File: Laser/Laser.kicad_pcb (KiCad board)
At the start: 2 copper layers, 25.4 x 25.4 mm, 2 parts, among them J1 Laser Diode, J2 Conn_01x03

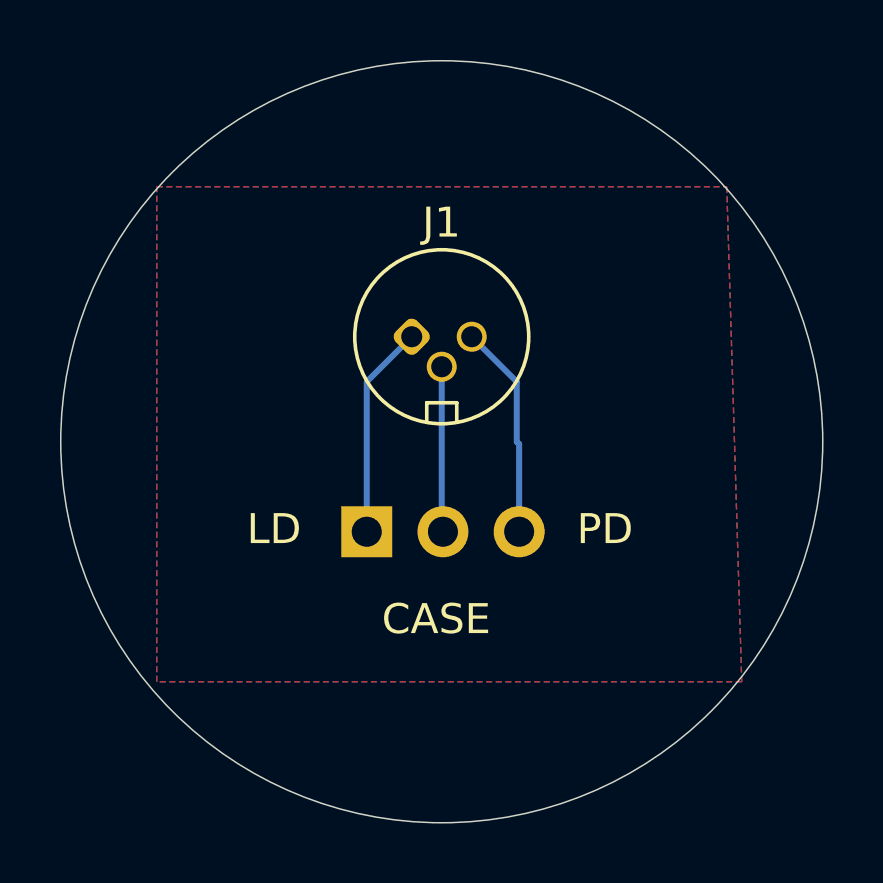
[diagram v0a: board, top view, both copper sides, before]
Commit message: Centering laser diode
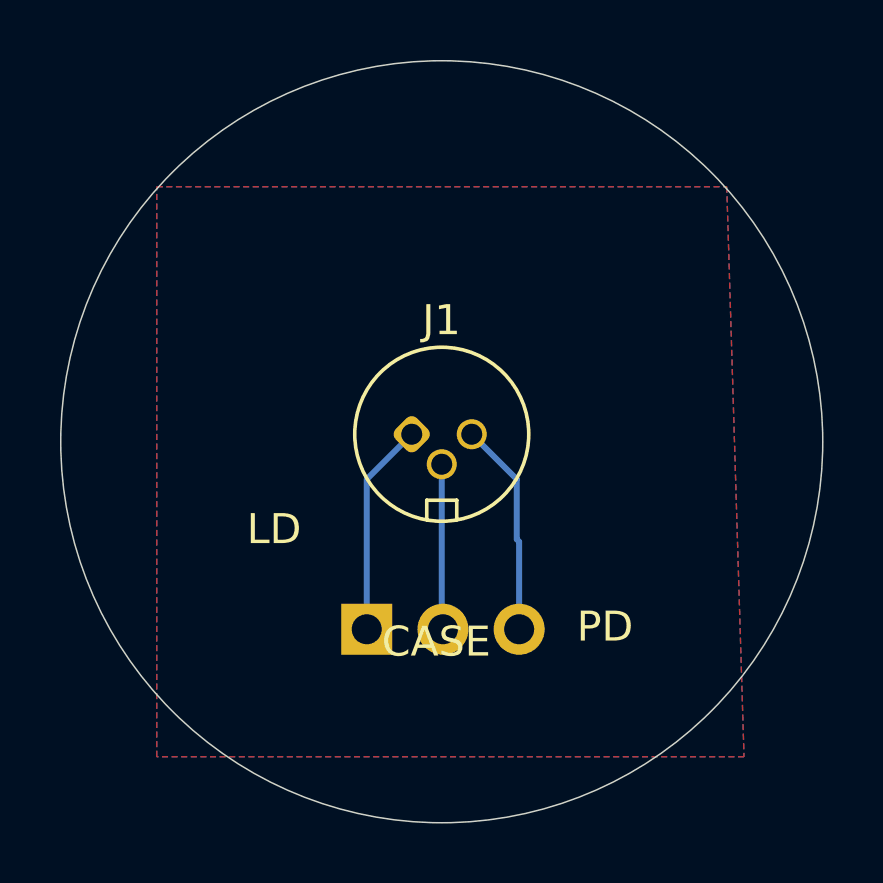
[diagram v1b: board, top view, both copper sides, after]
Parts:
- moved J1 3.25 mm to (155.5, 66.8)
- moved J2 3.25 mm to (154.0, 73.2)
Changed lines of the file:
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@@
 	(footprint "OptoDevice:LaserDiode_TO56-3"
 		(layer "F.Cu")
-		(at 155.5 63.5)
+		(at 155.5 66.75)
 		(descr "Laser Diode, TO-56, 3pin")
 		(tags "Laser Diode TO56")
@@
 	(footprint "Connector_PinHeader_2.54mm:PinHeader_1x03_P2.54mm_Vertical"
 		(layer "B.Cu")
-		(at 154 70 -90)
+		(at 154 73.25 -90)
 		(descr "Through hole straight pin header, 1x03, 2.54mm pitch, single row")
 		(tags "Through hole pin header THT 1x03 2.54mm single row")
@@
 	)
 	(gr_text "PD"
-		(at 161 70.5 0)
+		(at 161 73.75 0)
 		(layer "F.SilkS")
 		(effects
@@
 	)
 	(gr_text "CASE"
-		(at 154.5 73.5 0)
+		(at 154.5 74.25 0)
 		(layer "F.SilkS")
 		(effects
@@
 	)
 	(segment
-		(start 159.08 67.08)
-		(end 159.08 70)
+		(start 159.08 70.33)
+		(end 159.08 73.25)
 		(width 0.2)
 		(layer "B.Cu")
@@
 	)
 	(segment
-		(start 159 65)
-		(end 159 67)
+		(start 159 68.25)
+		(end 159 70.25)
 		(width 0.2)
 		(layer "B.Cu")
@@
 	)
 	(segment
-		(start 159 67)
-		(end 159.08 67.08)
+		(start 159 70.25)
+		(end 159.08 70.33)
 		(width 0.2)
 		(layer "B.Cu")
@@
 	)
 	(segment
-		(start 157.5 63.5)
-		(end 159 65)
+		(start 157.5 66.75)
+		(end 159 68.25)
 		(width 0.2)
 		(layer "B.Cu")
@@
 	)
 	(segment
-		(start 156.5 69.96)
-		(end 156.54 70)
+		(start 156.5 73.21)
+		(end 156.54 73.25)
 		(width 0.2)
 		(layer "B.Cu")
@@
 	)
 	(segment
-		(start 156.5 64.5)
-		(end 156.5 69.96)
+		(start 156.5 67.75)
+		(end 156.5 73.21)
 		(width 0.2)
 		(layer "B.Cu")
@@
 	)
 	(segment
-		(start 155.5 63.5)
-		(end 154 65)
+		(start 155.5 66.75)
+		(end 154 68.25)
 		(width 0.2)
 		(layer "B.Cu")
@@
 	)
 	(segment
-		(start 154 65)
-		(end 154 70)
+		(start 154 68.25)
+		(end 154 73.25)
 		(width 0.2)
 		(layer "B.Cu")
@@
 		(polygon
 			(pts
-				(xy 147 58.5) (xy 166 58.5) (xy 166.5 75) (xy 147 75)
+				(xy 147 58.5) (xy 166 58.5) (xy 166.575758 77.5) (xy 147 77.5)
 			)
 		)
@@
 		(polygon
 			(pts
-				(xy 147 58.5) (xy 166 58.5) (xy 166.5 75) (xy 147 75)
-			)
-		)
+				(xy 147 58.5) (xy 166 58.5) (xy 166.575758 77.5) (xy 147 77.5)
+			)
+		)
